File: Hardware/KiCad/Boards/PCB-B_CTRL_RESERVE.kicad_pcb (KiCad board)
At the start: 2 copper layers, 180 x 94 mm, 0 parts

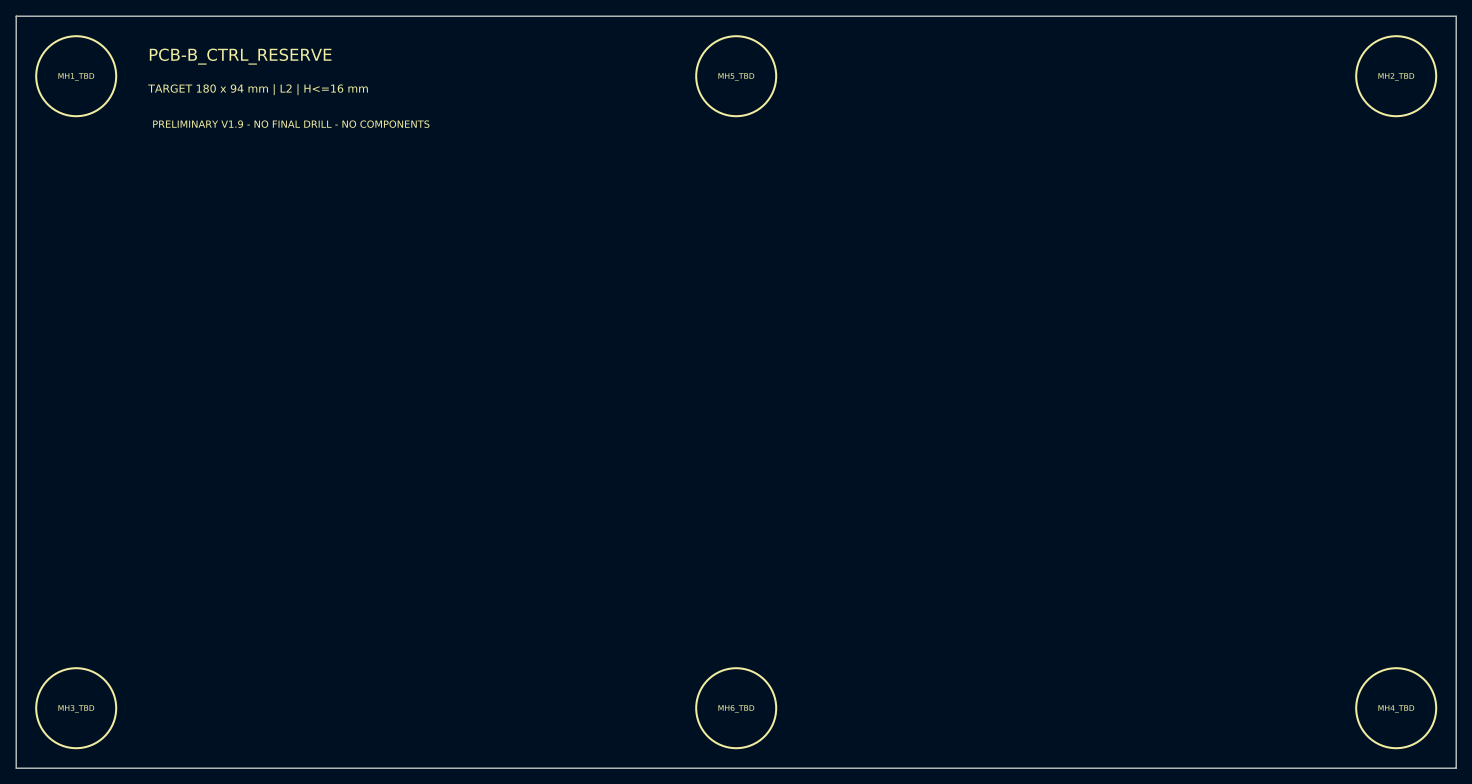
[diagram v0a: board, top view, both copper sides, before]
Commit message: hardware: add PCB-B functional, height and connector placeholders
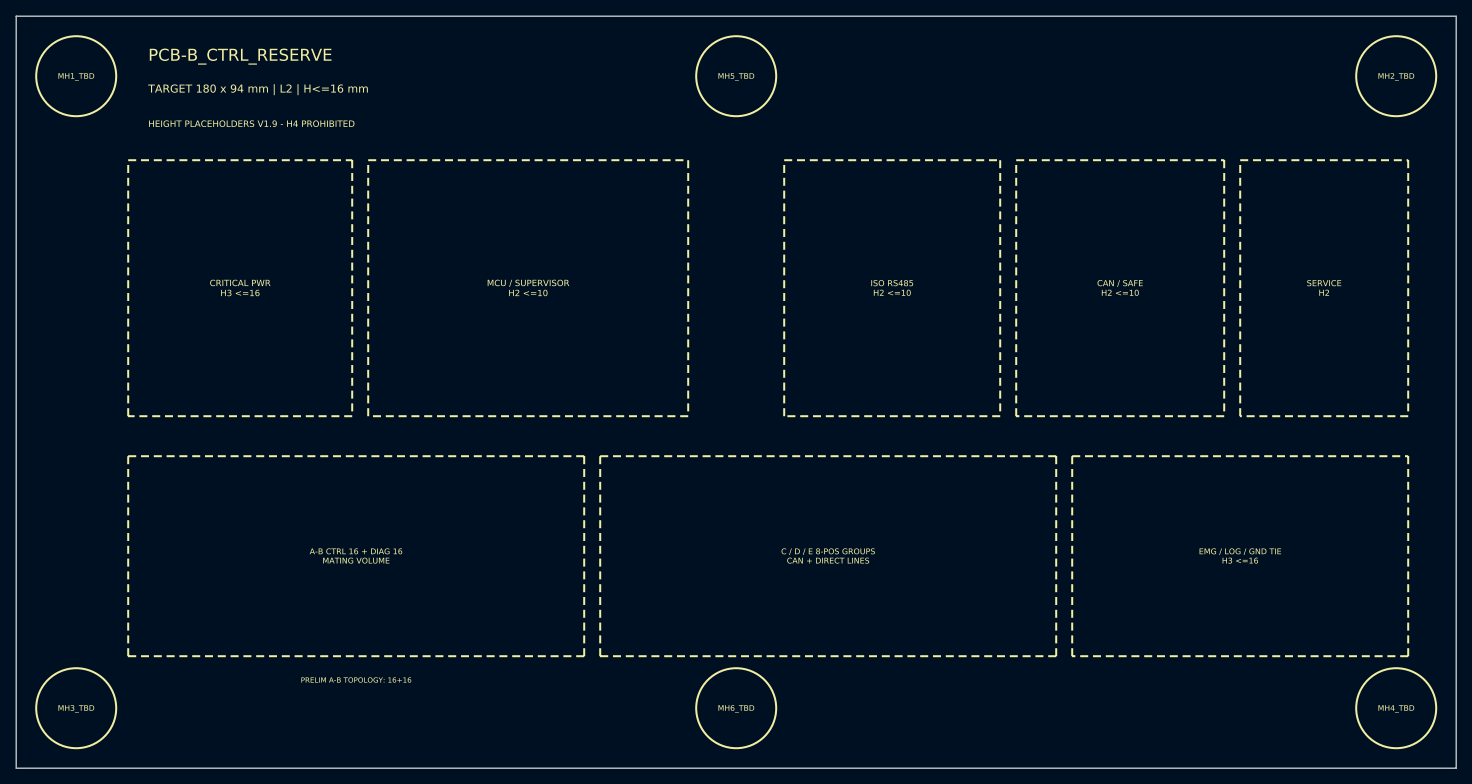
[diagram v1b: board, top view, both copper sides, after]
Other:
- board text added: "A-B CTRL 16 + DIAG 16 MATING VOLUME"
- board text added: "C / D / E 8-POS GROUPS CAN + DIRECT LINES"
- board text added: "CAN / SAFE H2 <=10"
- board text added: "CRITICAL PWR H3 <=16"
- board text added: "EMG / LOG / GND TIE H3 <=16"
- board text added: "HEIGHT PLACEHOLDERS V1.9 - H4 PROHIBITED"
- board text added: "ISO RS485 H2 <=10"
- board text added: "MCU / SUPERVISOR H2 <=10"
- board text added: "PRELIM A-B TOPOLOGY: 16+16"
- board text added: "SERVICE H2"
- board text removed: "PRELIMINARY V1.9 - NO FINAL DRILL - NO COMPONENTS"
